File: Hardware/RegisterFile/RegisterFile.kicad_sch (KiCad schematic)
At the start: 23 parts, among them J1 Conn_02x08_Odd_Even, J2 Conn_02x08_Odd_Even, J3 Conn_02x08_Odd_Even, J4 Conn_02x08_Odd_Even

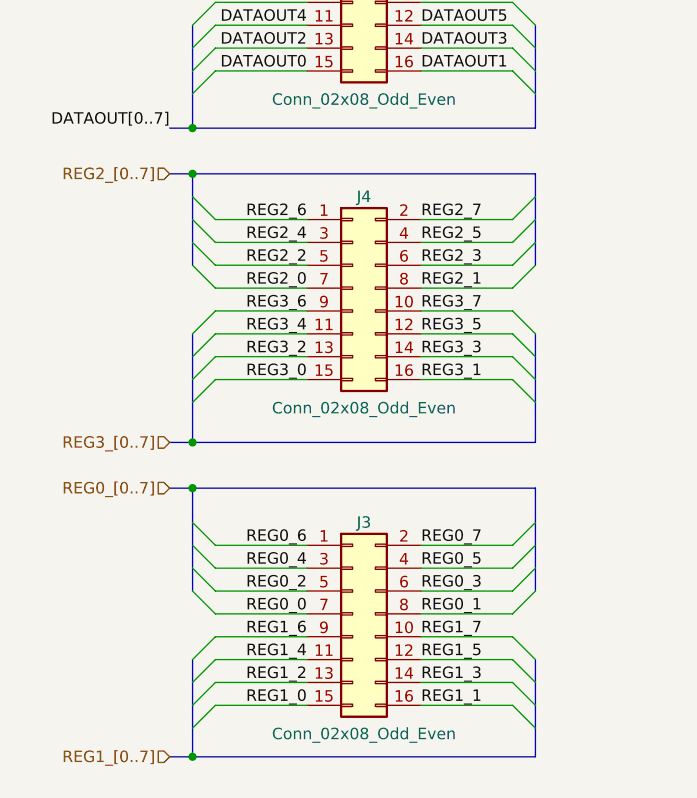
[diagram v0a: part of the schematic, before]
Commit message: Motherboard Significant Progress
This involves significant buildup of the motherboard, such as the power, oscillator, and overall design.

The motherboard schematic is in progress (some lines have yet to be connected), and the PCB layout is mostly just there to consider spacing.
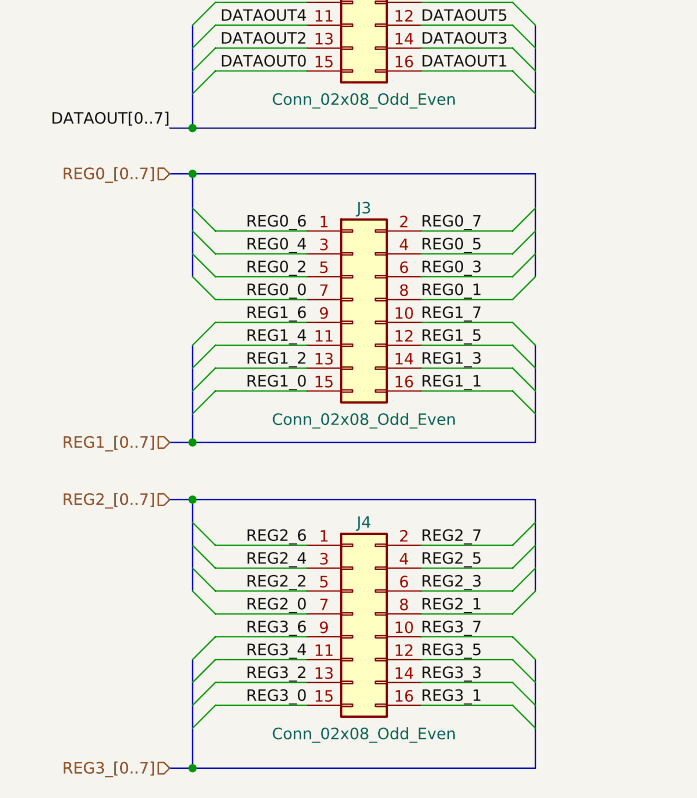
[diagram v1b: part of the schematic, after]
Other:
- moved on the sheet: J3, J4
